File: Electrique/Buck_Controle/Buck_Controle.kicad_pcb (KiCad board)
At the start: 2 copper layers, 10 parts, among them U1 TPS5450DDA

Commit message: Continuation PCB controle
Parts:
- added G***: LOGO, Robotique_UdeS_Logos_KiCad:Logo_RobotiqueUdeS_PCB_small, B.Cu at (222.2, 76.2)
- added REF**: MountingHole_2.2mm_M2, MountingHole:MountingHole_2.2mm_M2, F.Cu at (233.7, 96.4)
- added REF**: MountingHole_2.2mm_M2, MountingHole:MountingHole_2.2mm_M2, F.Cu at (199.8, 96.4)
- added REF**: MountingHole_2.2mm_M2, MountingHole:MountingHole_2.2mm_M2, F.Cu at (233.7, 70.0)
- added REF**: MountingHole_2.2mm_M2, MountingHole:MountingHole_2.2mm_M2, F.Cu at (199.8, 70.0)
- moved Rfbb1 6.83 mm to (198.9, 88.3), turned to 0 degrees
- moved Rfbt1 5.57 mm to (198.1, 91.1)
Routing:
- net GND: track 0.00 -> 1.50 mm
- added copper zone on F.Cu, net +BATT
- added copper zone on F.Cu, net /Vout
- added copper zone on F.Cu, net GND
- added copper zone on F.Cu, net Net-(Cboot1-Pad1)
- added copper zone on F.Cu, net Net-(Cboot1-Pad2)
- added copper zone on F.Cu, net Net-(Rfbb1-Pad1)
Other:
- board outline added: 40 x 32.5 mm
- board text added: "Buck Converter 12V-5V"

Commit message: Ajout pieces manquantes Boost
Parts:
- added G***: LOGO, KiCad_Divers:RoverOfficialLogo, B.Cu at (204.5, 92.6)

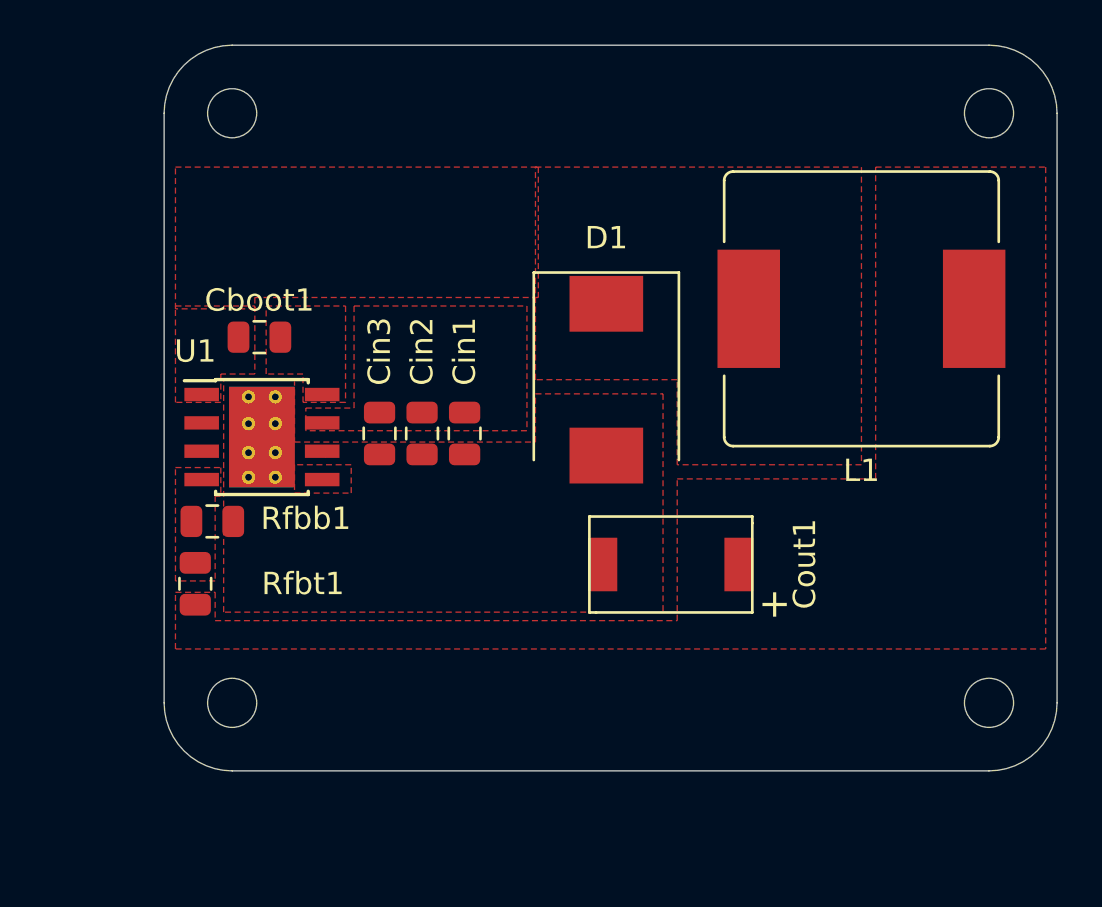
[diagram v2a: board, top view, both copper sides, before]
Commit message: Ajout du bus in/out
Ajout du bus pour in/out + routage sur la couche du dessous + via pour transférer ces signaux sur les 2 couches
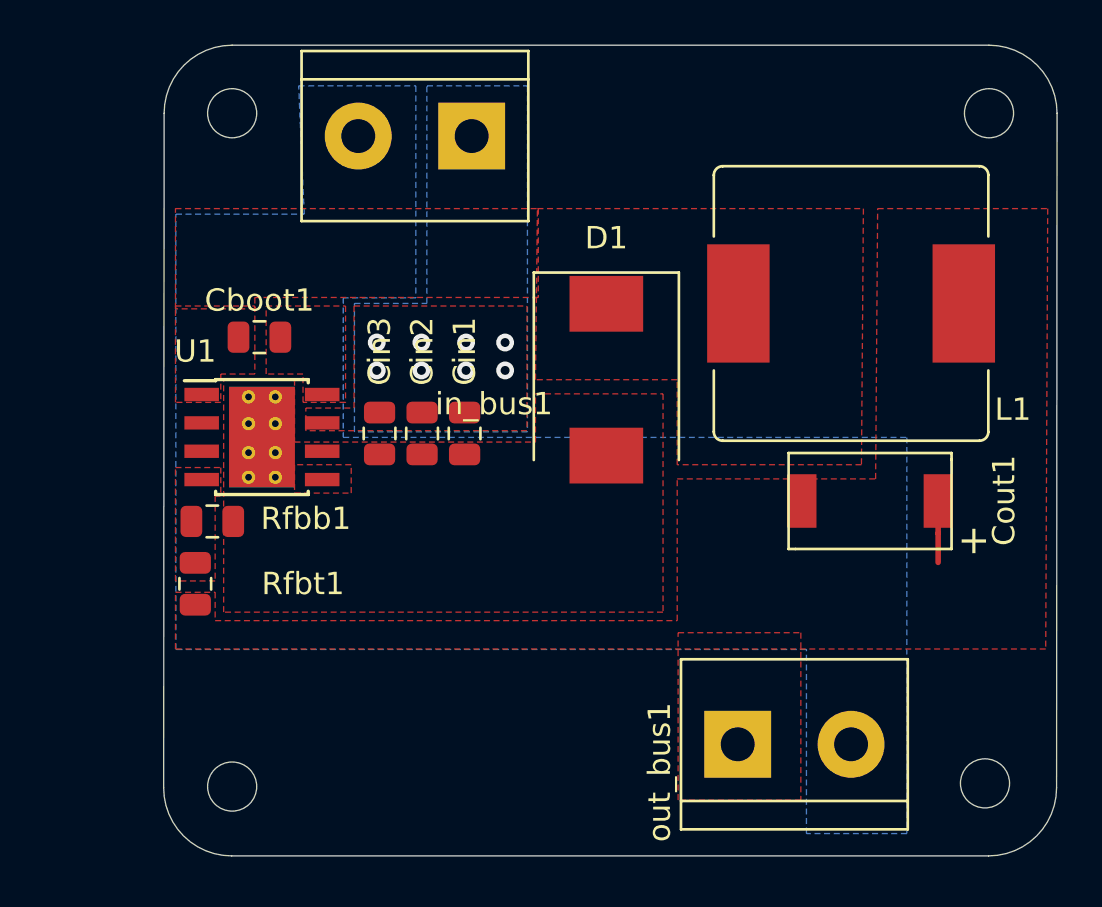
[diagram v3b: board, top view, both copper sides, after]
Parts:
- added in_bus1: Screw_Terminal_01x02, TerminalBlock:TerminalBlock_bornier-2_P5.08mm, F.Cu at (210.5, 71.0)
- added out_bus1: Screw_Terminal_01x02, TerminalBlock:TerminalBlock_bornier-2_P5.08mm, F.Cu at (222.4, 98.2)
- moved Cout1 9.37 mm to (228.0, 90.5)
- moved REF** 3.75 mm to (199.8, 100.1)
- moved REF** 3.61 mm to (233.5, 100.0)
- moved L1 0.52 mm to (227.5, 78.5)
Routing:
- net /Vout: track 0.00 -> 2.75 mm
- net +BATT: vias 0 -> 8
- added copper zone on B.Cu, net +BATT
- added copper zone on B.Cu, net GND
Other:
- board size 40 x 32.5 mm -> 40 x 36.3 mm

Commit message: Changement du branchement de Cboot + DRC pcb controle
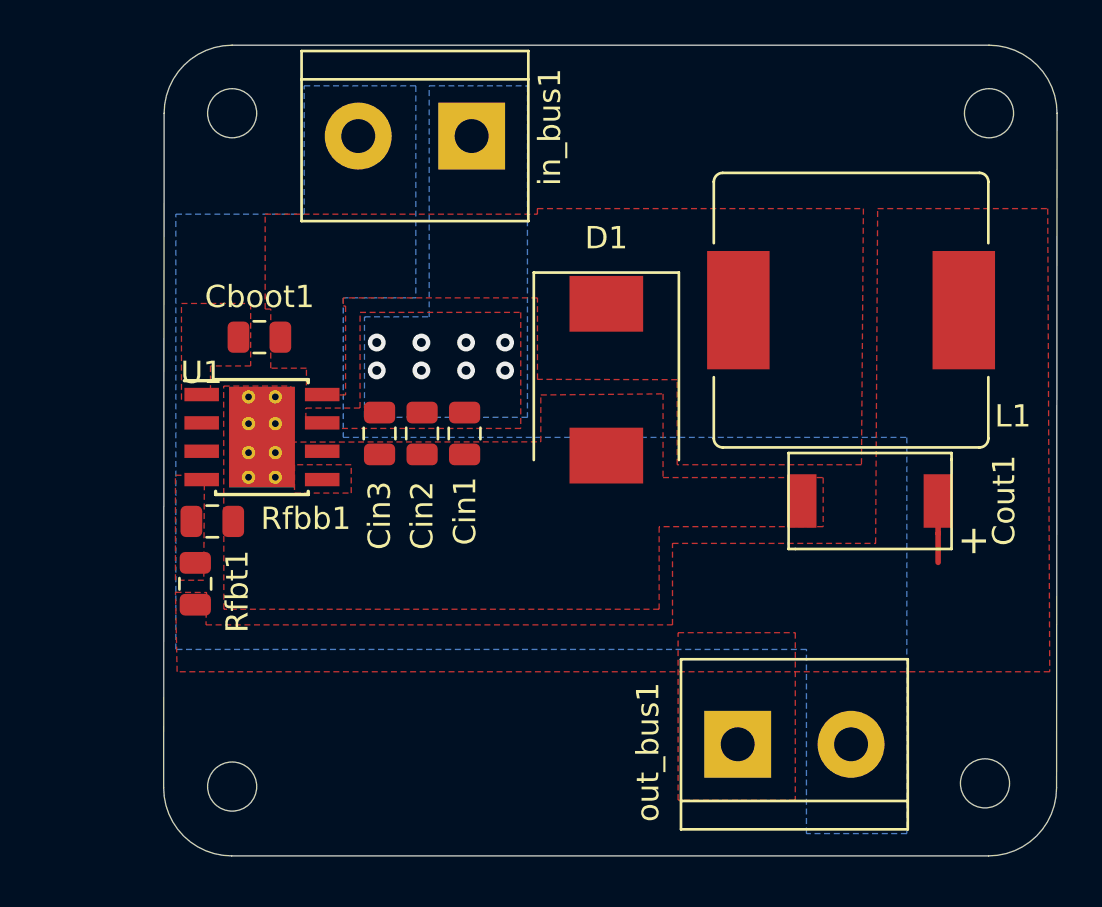
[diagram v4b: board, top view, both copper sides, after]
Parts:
- moved L1 0.30 mm to (227.5, 78.8)
- turned Cboot1 to 180 degrees
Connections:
- U1 pad 1: Net-(Cboot1-Pad1) -> Net-(Cboot1-Pad2)
- U1 pad 8: Net-(Cboot1-Pad2) -> Net-(Cboot1-Pad1)
